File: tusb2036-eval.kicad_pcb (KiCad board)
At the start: 2 copper layers, 85 x 52 mm, 49 parts, among them J1 USB_B_Micro, J2 USB_A, J3 USB_A, J4 USB_A, SW1 RESET, U1 TUSB2036, U2 TPS76333, U3 TPS2044D, U4 SN75240, U5 SN75240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

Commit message: Add test points
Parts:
- added TP1: GND, TestPoint:TestPoint_Pad_D2.0mm, F.Cu at (101.5, 75.0)
- added TP2: 5V, TestPoint:TestPoint_Pad_D2.0mm, F.Cu at (106.5, 78.5)
- added TP3: 5VA, TestPoint:TestPoint_Pad_D2.0mm, F.Cu at (117.0, 107.0)
- added TP4: 5VB, TestPoint:TestPoint_Pad_D2.0mm, F.Cu at (142.0, 107.0)
- added TP5: 5VC, TestPoint:TestPoint_Pad_D2.0mm, F.Cu at (165.0, 107.0)
- moved J1 3.05 mm to (103.2, 122.2)
- renumbered TP1 to TP6
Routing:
- net VBUS: track 121.3 -> 135.8 mm
- net /U0+: track 16.6 -> 20.0 mm
- net GND: track 130.4 -> 128.5 mm, vias 27 -> 26
- net /U0-: track 19.8 -> 21.5 mm

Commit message: Fix button footprint and other small updates
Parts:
- SW1: footprint Button_Switch_SMD:SW_SPST_Omron_B3FS-100xP -> Omron:SW_SPST_Omron_B3FS-100xP
- turned SW1 to 0 degrees
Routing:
- net Net-(SW1-Pad2): track 39.4 -> 47.7 mm
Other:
- board text added: "HI"
- board text added: "LO"
- board text added: "TUSB2036 USB Hub Evaluation Board v4 C. Keller 2021-04-18"
- board text removed: "TUSB2036 USB Hub Evaluation Board v4 C. Keller 2021-04-14"

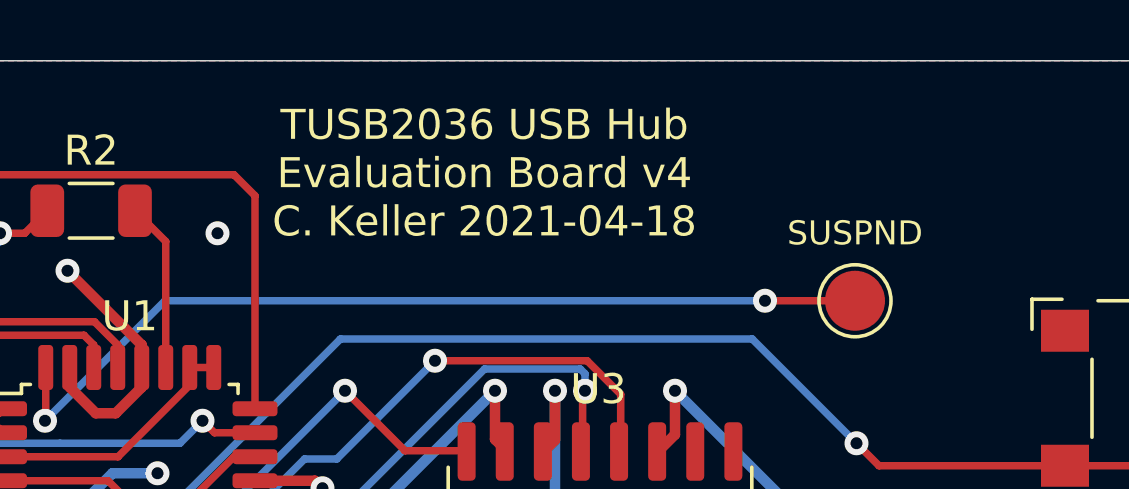
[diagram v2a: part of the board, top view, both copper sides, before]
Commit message: Adjust silkscreen
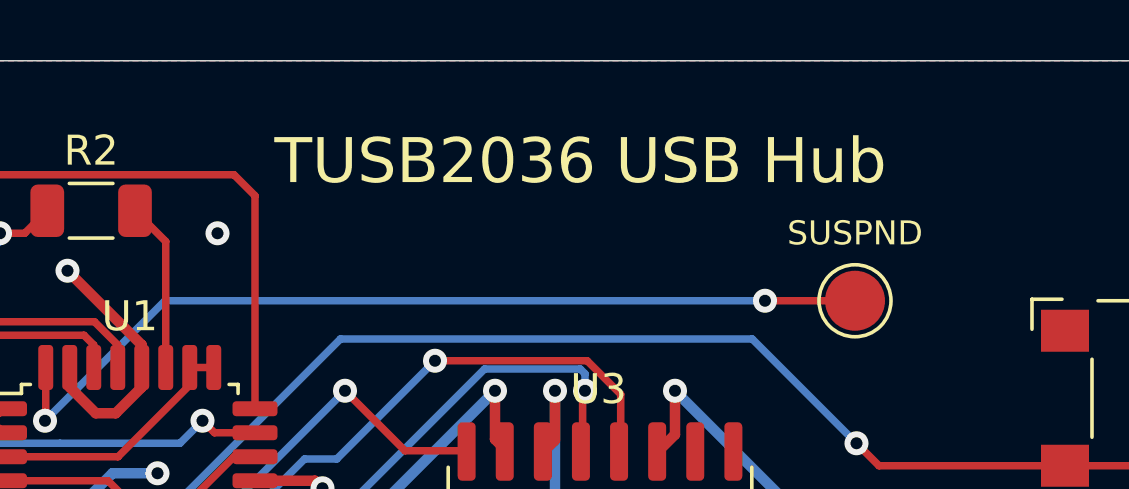
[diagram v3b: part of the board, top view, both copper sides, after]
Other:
- board text added: "TUSB2036 USB Hub"
- board text added: "TUSB2036 USB Hub Evaluation Board v4 C. Keller 2021-04-18 https://github.com/k0swe/tusb2036-eval"
- board text removed: "TUSB2036 USB Hub Evaluation Board v4 C. Keller 2021-04-18"
- board text removed: "https://github.com/k0swe/tusb2036-eval"

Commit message: Add OSHW logo
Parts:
- added LOGO1: Logo_Open_Hardware_Small, Symbol:OSHW-Logo2_9.8x8mm_SilkScreen, B.Cu at (113.0, 101.0)

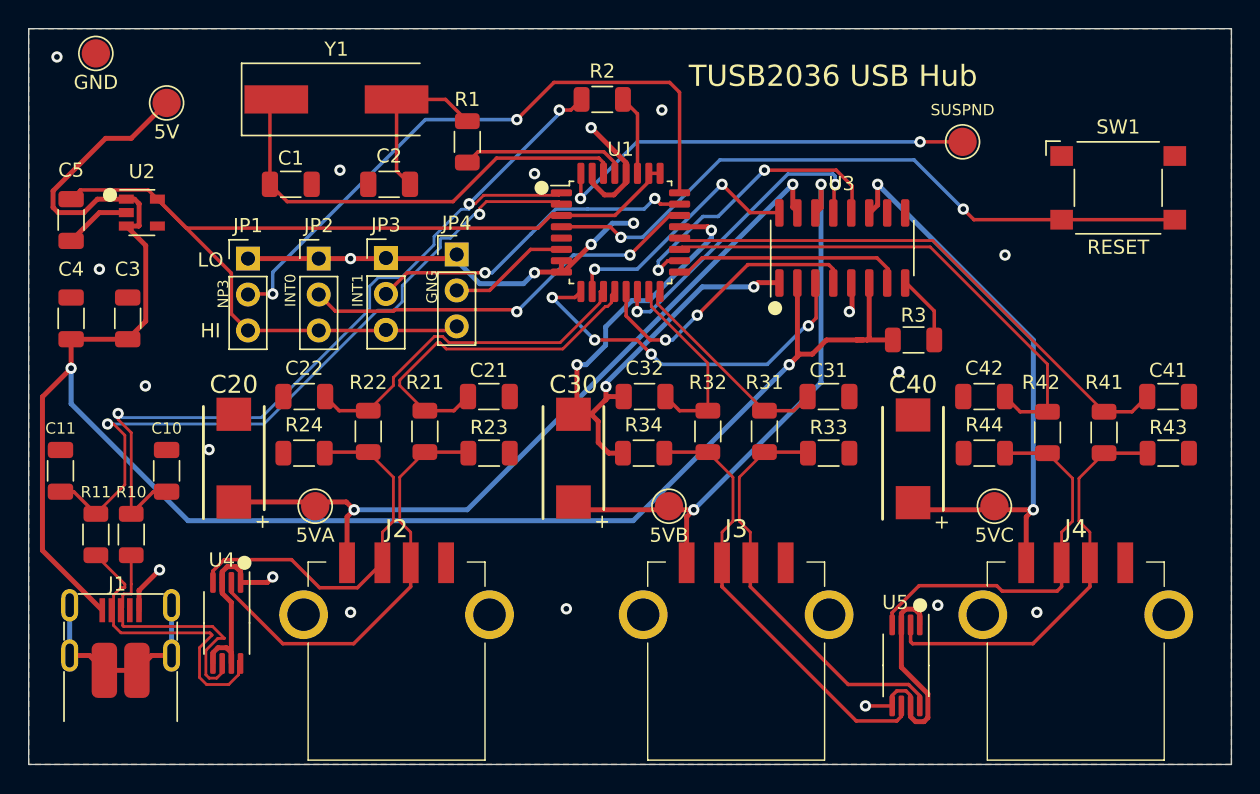
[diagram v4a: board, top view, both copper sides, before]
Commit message: Add LEDs
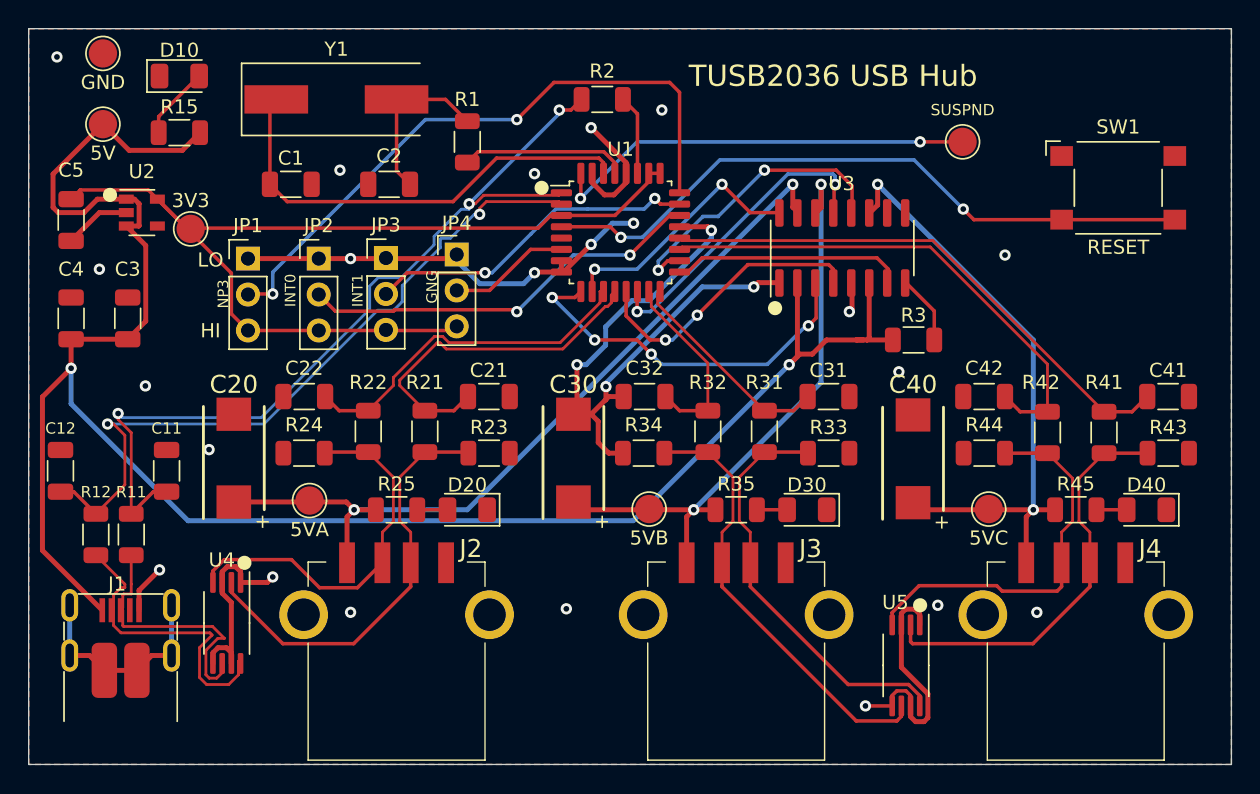
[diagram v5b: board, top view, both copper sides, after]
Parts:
- added D10: VBUS, LED_SMD:LED_1206_3216Metric, F.Cu at (107.4, 76.6)
- added D20: 5VA, LED_SMD:LED_1206_3216Metric, F.Cu at (127.8, 107.2)
- added D30: 5VB, LED_SMD:LED_1206_3216Metric, F.Cu at (151.8, 107.2)
- added D40: 5VC, LED_SMD:LED_1206_3216Metric, F.Cu at (175.8, 107.2)
- added R15: 330Ω, Resistor_SMD:R_1206_3216Metric, F.Cu at (107.4, 80.6)
- added R25: 330Ω, Resistor_SMD:R_1206_3216Metric, F.Cu at (122.8, 107.2)
- added R35: 330Ω, Resistor_SMD:R_1206_3216Metric, F.Cu at (146.8, 107.2)
- added R45: 330Ω, Resistor_SMD:R_1206_3216Metric, F.Cu at (170.8, 107.2)
- added TP7: 3V3, TestPoint:TestPoint_Pad_D2.0mm, F.Cu at (108.2, 87.4)
- R1: value 27Ω -> 1.5kΩ
- moved TP2 4.74 mm to (102.0, 80.0)
- moved TP4 1.41 mm to (140.6, 107.2)
- moved TP3 0.57 mm to (116.6, 106.6)
- moved TP1 0.50 mm to (102.0, 75.0)
- moved TP5 0.45 mm to (164.6, 107.2)
- renumbered C10 to C11, C11 to C12, R10 to R11, R11 to R12
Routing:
- net Net-(D10-Pad2): track 0.00 -> 5.19 mm
- net VBUS: track 135.8 -> 139.5 mm
- net Net-(D40-Pad2): track 0.00 -> 2.14 mm
- net Net-(D30-Pad2): track 0.00 -> 2.14 mm
- net Net-(D20-Pad2): track 0.00 -> 2.14 mm
- net /5VC: track 42.8 -> 44.3 mm
- net /5VA: track 55.5 -> 57.1 mm
- net /5VB: track 41.9 -> 43.1 mm

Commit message: Implement overcurrent resistor changes
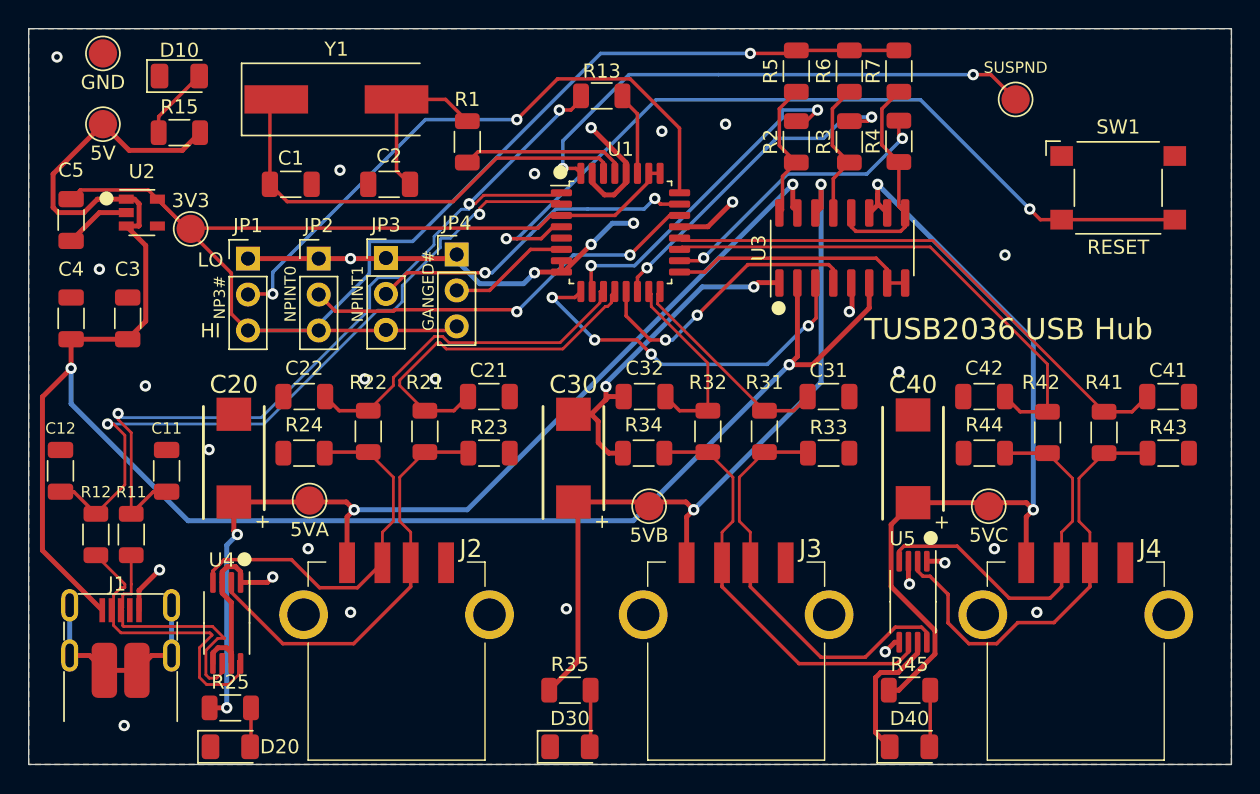
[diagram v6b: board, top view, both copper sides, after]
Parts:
- added R13: 1.5kΩ, Resistor_SMD:R_1206_3216Metric, F.Cu at (137.2, 78.0)
- added R4: 15kΩ, Resistor_SMD:R_1206_3216Metric, F.Cu at (158.2, 81.2)
- added R5: 15kΩ, Resistor_SMD:R_1206_3216Metric, F.Cu at (151.0, 76.2)
- added R6: 15kΩ, Resistor_SMD:R_1206_3216Metric, F.Cu at (154.8, 76.2)
- added R7: 15kΩ, Resistor_SMD:R_1206_3216Metric, F.Cu at (158.2, 76.2)
- JP1: value NP3_SEL -> NP3#
- JP2: value NPINT0_SEL -> NPINT0
- JP3: value NPINT1_SEL -> NPINT1
- JP4: value GANGED_SEL -> GANGED#
- R2: value 1.5kΩ -> 15kΩ
- moved D20 23.7 mm to (111.0, 124.0), turned to 0 degrees
- moved D30 23.7 mm to (135.0, 124.0), turned to 0 degrees
- moved D40 23.7 mm to (159.0, 124.0), turned to 0 degrees
- moved R25 18.3 mm to (111.0, 121.2)
- moved R35 17.3 mm to (135.0, 120.0)
- moved R45 17.3 mm to (159.0, 120.0)
- moved R3 14.7 mm to (154.8, 81.2), turned to 90 degrees
- moved R2 14.0 mm to (151.0, 81.2), turned to 90 degrees
- moved TP6 4.80 mm to (166.5, 78.2)
- moved U5 4.53 mm to (159.2, 113.8)
- moved TP4 0.20 mm to (140.6, 107.0)
- moved TP5 0.20 mm to (164.6, 107.0)
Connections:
- net /EN1 renamed /EN1#
- net /EN2 renamed /EN2#
- net /GANGED renamed /GANGED#
- net /NP3 renamed /NP3#
- R2 pad 2: /D0+ -> /OC1#
- R3 pad 2: VBUS -> /OC2#
- U1 pad 10: /OC1 -> /OC1#
- U1 pad 14: /OC2 -> /OC2#
- U1 pad 17: /EN3 -> /EN3#
- U1 pad 18: /OC3 -> /OC3#
- U1 pad 27: Net-(R2-Pad1) -> Net-(R13-Pad1)
- U3 pad 10: (no net) -> /5VC
- U3 pad 12: /OC3 -> Net-(R4-Pad1)
- U3 pad 13: /OC2 -> Net-(R3-Pad1)
- U3 pad 16: /OC1 -> Net-(R2-Pad1)
- U3 pad 7: /EN3 -> /EN3#
- U3 pad 8: Net-(R3-Pad1) -> /EN3#
- U3 pad 9: (no net) -> Net-(R4-Pad1)
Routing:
- net +3V3: track 71.8 -> 127.3 mm, vias 0 -> 1
- net /OC1#: track 0.00 -> 24.6 mm, vias 0 -> 2
- net /OC2#: track 0.00 -> 24.0 mm, vias 0 -> 2
- net /OC2: track 22.1 -> 0.00 mm, vias 2 -> 0
- net /OC3: track 21.1 -> 0.00 mm, vias 2 -> 0
- net /OC3#: track 0.00 -> 20.7 mm, vias 0 -> 2
- net GND: track 128.5 -> 108.8 mm, vias 26 -> 32
- net /OC1: track 18.1 -> 0.00 mm, vias 2 -> 0
- net /5VC: track 44.3 -> 62.0 mm
- net /EN3#: track 0.00 -> 17.6 mm
- net /EN3: track 16.4 -> 0.00 mm
- net Net-(R4-Pad1): track 0.00 -> 15.8 mm
- net /5VA: track 57.1 -> 71.7 mm, vias 2 -> 4
- net /5VB: track 43.1 -> 56.6 mm
- net Net-(SW1-Pad2): track 47.7 -> 59.1 mm
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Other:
- board text added: "TUSB2036 USB Hub Evaluation Board v4 C. Keller 2021-04-28 https://github.com/k0swe/tusb2036-eval"
- board text removed: "GNG"
- board text removed: "INT0"
- board text removed: "INT1"
- board text removed: "NP3"
- board text removed: "TUSB2036 USB Hub Evaluation Board v4 C. Keller 2021-04-18 https://github.com/k0swe/tusb2036-eval"

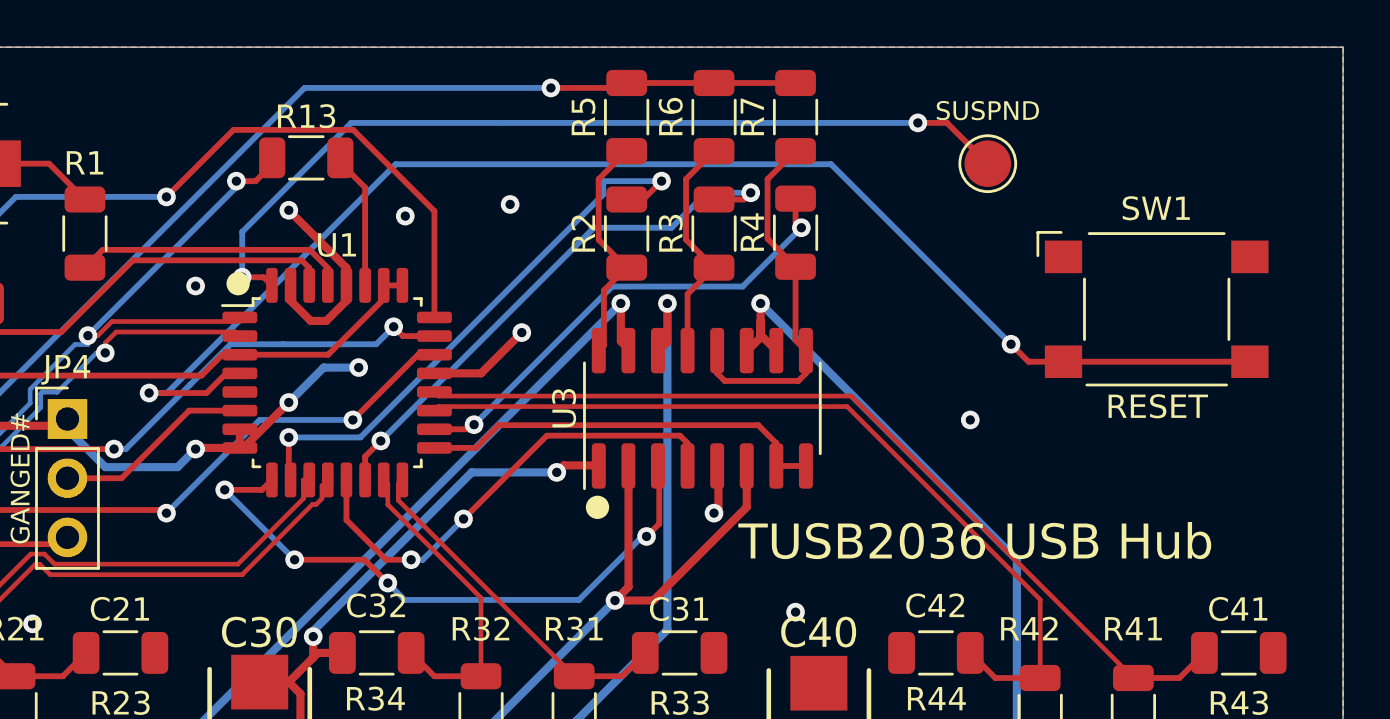
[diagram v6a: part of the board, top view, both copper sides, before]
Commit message: Add RC filter for RESET
Suggested by eevblog user pigrew and example schematic
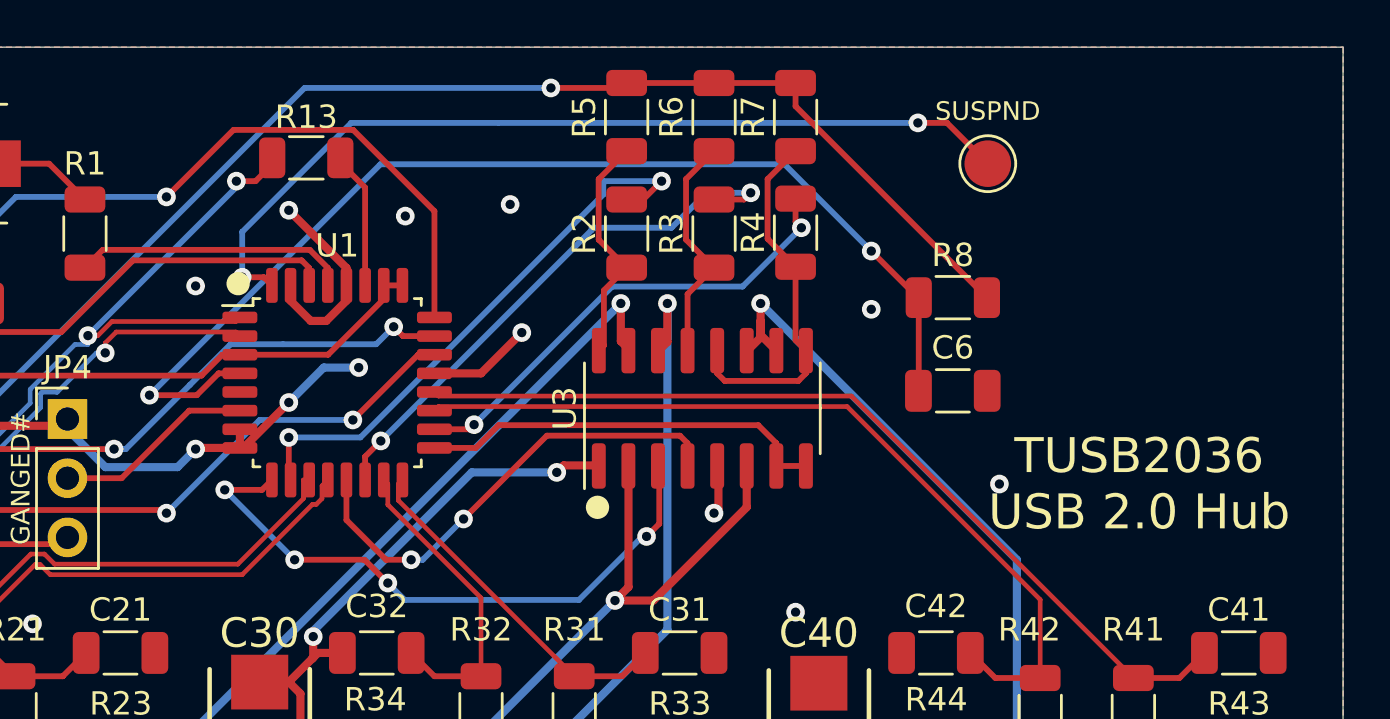
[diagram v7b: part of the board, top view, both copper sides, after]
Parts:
- removed SW1: RESET, Omron:SW_SPST_Omron_B3FS-100xP
- added C6: 0.1μF, Capacitor_SMD:C_1206_3216Metric, F.Cu at (165.0, 88.0)
- added R8: 15kΩ, Resistor_SMD:R_1206_3216Metric, F.Cu at (165.0, 84.0)
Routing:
- net +3V3: track 127.3 -> 139.9 mm
- net Net-(C6-Pad1): track 59.1 -> 47.8 mm
- net GND: vias 32 -> 33
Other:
- board text added: "TUSB2036 USB 2.0 Hub"
- board text added: "TUSB2036 USB Hub Evaluation Board v4 C. Keller 2021-05-04 https://github.com/k0swe/tusb2036-eval"
- board text removed: "TUSB2036 USB Hub"
- board text removed: "TUSB2036 USB Hub Evaluation Board v4 C. Keller 2021-04-28 https://github.com/k0swe/tusb2036-eval"
